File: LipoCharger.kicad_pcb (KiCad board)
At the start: 2 copper layers, 18 parts, among them J1 S2B-XH-A, J2 USB_C_Receptacle_USB2.0_14P, Q1 2300A, Q2 2300A, U1 TP4056-42-ESOP8, U2 DW01A

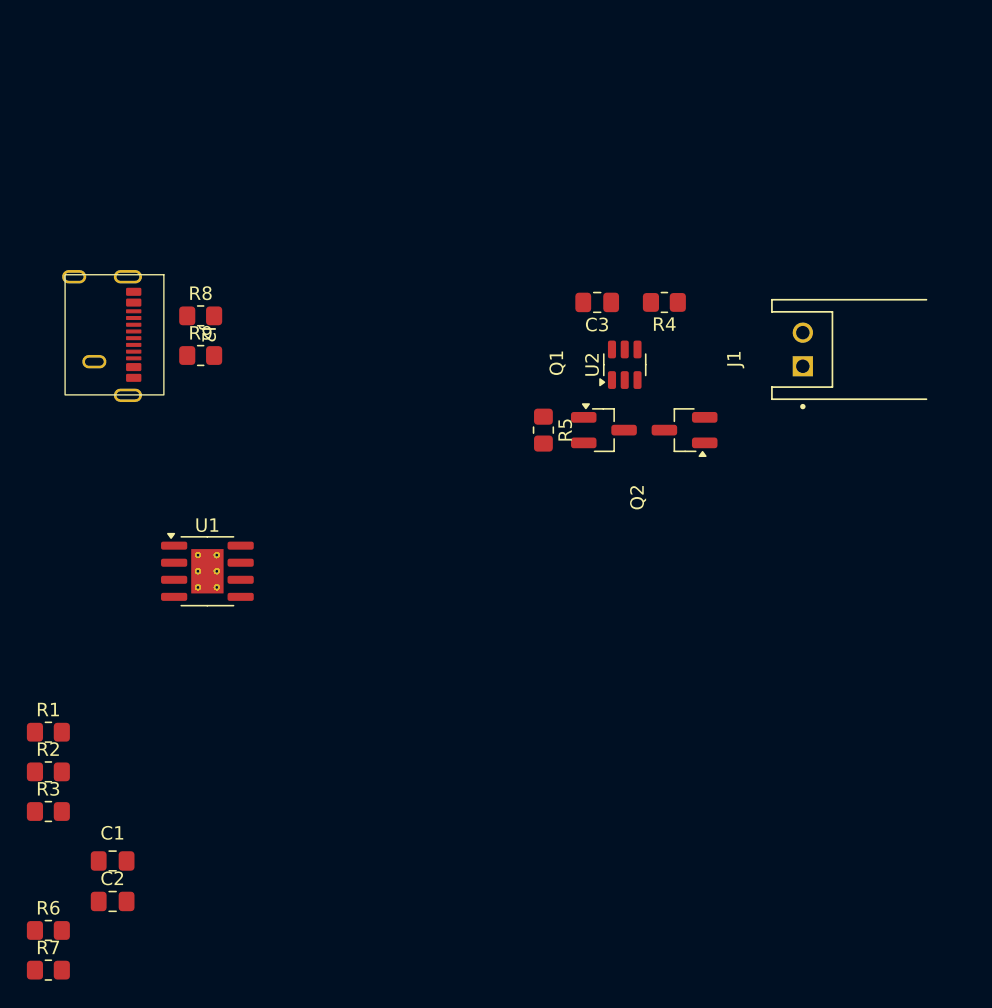
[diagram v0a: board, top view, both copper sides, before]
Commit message: Replaced the DW01 with a FM2113
The DW01 was not suited for a LIPO battery, the under voltage threshold was too low, so it was replaced with the FM2113 which has a much higher threshold
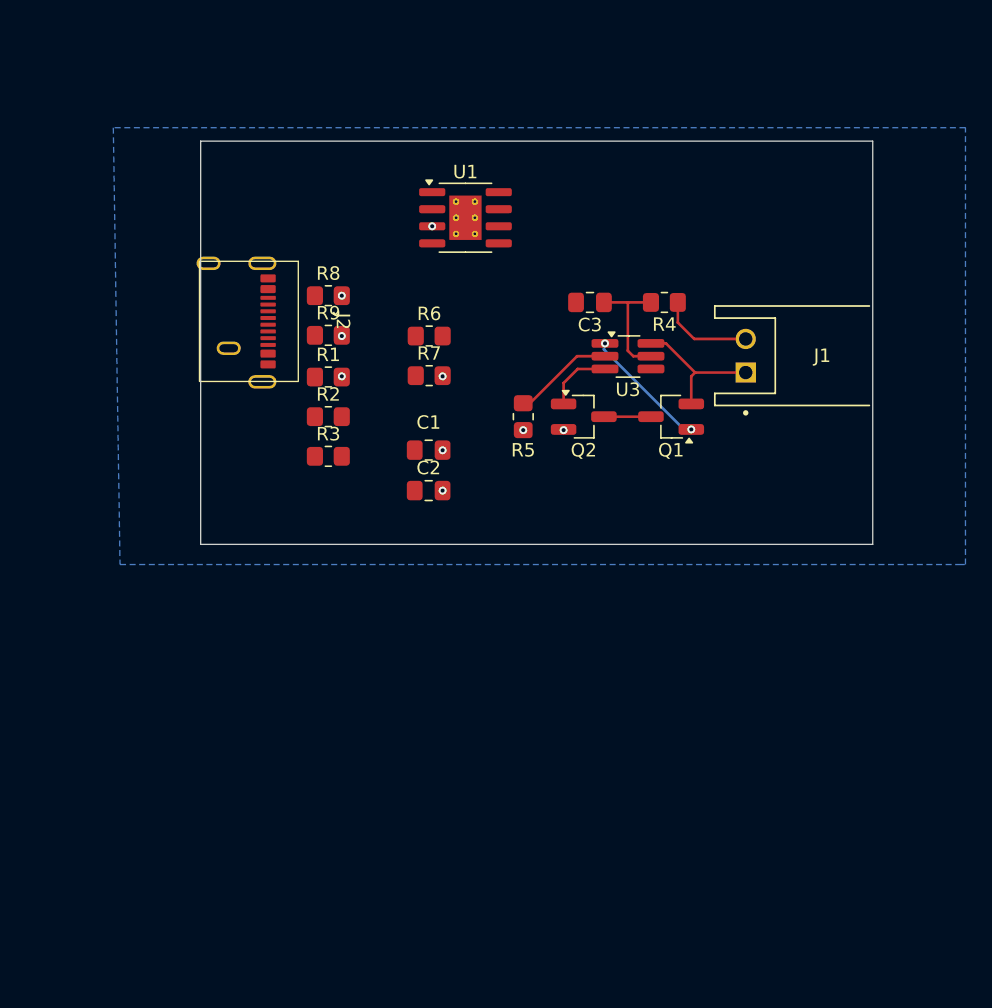
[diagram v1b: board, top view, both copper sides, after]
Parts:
- removed U2: DW01A, Package_TO_SOT_SMD:SOT-23-6
- added U3: FM2113, Package_TO_SOT_SMD:TSOT-23-6_HandSoldering, F.Cu at (61.8, 46.0)
- R5: value 1k -> 2k
- moved R6 52.5 mm to (47.0, 44.5)
- moved R7 52.5 mm to (47.0, 47.5)
- moved C1 38.6 mm to (47.0, 53.0)
- moved C2 38.6 mm to (47.0, 56.0)
- moved R1 33.6 mm to (39.5, 47.5)
- moved R2 33.6 mm to (39.5, 50.5)
- moved R3 33.6 mm to (39.5, 53.5)
- moved U1 32.6 mm to (49.7, 35.7)
- moved J2 10.0 mm to (35.6, 43.4)
- moved R8 9.62 mm to (39.5, 41.5)
- moved R9 9.62 mm to (39.5, 44.5)
- moved Q2 7.57 mm to (58.5, 50.5), turned to 0 degrees
- moved Q1 5.10 mm to (65.0, 50.5), turned to 180 degrees
- moved J1 4.28 mm to (76.2, 46.0)
- moved R5 1.80 mm to (54.0, 50.5)
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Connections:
- net -BATT renamed GND
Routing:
- net Net-(Q1-S): track 0.00 -> 10.4 mm
- net Net-(Q1-G): track 0.00 -> 9.57 mm, vias 0 -> 2
- net Net-(U3-VDD): track 0.00 -> 8.98 mm
- net Net-(U3-CS): track 0.00 -> 7.53 mm
- net +BATT: track 0.00 -> 7.05 mm
- net Net-(Q2-G): track 0.00 -> 5.06 mm
- net Net-(Q1-D): track 0.00 -> 3.50 mm
- net GND: track 0.00 -> 0.28 mm, vias 0 -> 9
- added copper zone on B.Cu, net GND
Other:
- board outline added: 50 x 30 mm

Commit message: Updated usb-c connector, added the 5v switcher, and started to find specific components for the swithcher
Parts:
- added C4: 22uF, Capacitor_SMD:C_0603_1608Metric_Pad1.08x0.95mm_HandSolder, F.Cu at (33.2, 48.8)
- added C5: 22uF, Capacitor_SMD:C_0603_1608Metric_Pad1.08x0.95mm_HandSolder, F.Cu at (33.2, 51.4)
- added D1: RED, LED_SMD:LED_0603_1608Metric_Pad1.05x0.95mm_HandSolder, F.Cu at (41.6, 57.0)
- added D2: GREEN, LED_SMD:LED_0603_1608Metric_Pad1.05x0.95mm_HandSolder, F.Cu at (37.6, 57.0)
- added D3: SS34, Diode_SMD:D_SMA-SMB_Universal_Handsoldering, F.Cu at (63.0, 33.9)
- added H1: MountingHole_Pad, MountingHole:MountingHole_2.2mm_M2_DIN965_Pad, F.Cu at (76.3, 36.9)
- added H2: MountingHole_Pad, MountingHole:MountingHole_2.2mm_M2_DIN965_Pad, F.Cu at (75.5, 55.2)
- added R10: 73.2k, Resistor_SMD:R_0603_1608Metric_Pad0.98x0.95mm_HandSolder, F.Cu at (33.2, 53.9)
- added R11: 10k, Resistor_SMD:R_0603_1608Metric_Pad0.98x0.95mm_HandSolder, F.Cu at (33.2, 56.4)
- added U2: MT3608, Package_TO_SOT_SMD:SOT-23-6, F.Cu at (71.2, 36.8)
- C1, C2, C3: footprint Capacitor_SMD:C_0805_2012Metric_Pad1.18x1.45mm_HandSolder -> Capacitor_SMD:C_0603_1608Metric_Pad1.08x0.95mm_HandSolder
- R1, R2, R3, R4, R5, R6, R7, R8, R9: footprint Resistor_SMD:R_0805_2012Metric_Pad1.20x1.40mm_HandSolder -> Resistor_SMD:R_0603_1608Metric_Pad0.98x0.95mm_HandSolder
- moved J2 3.37 mm to (38.0, 41.0)

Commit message: Cleaned up schematic and added a slide switch
* Added a slide switch for enabling the 5v Switcher
* Added the USB protection and part numbers
* Consolidated all of the symbols into the Symbols folder (instead of the _Library.pretty folder)
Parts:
- added D6: 5.1v, Diode_SMD:Nexperia_CFP3_SOD-123W, F.Cu at (53.1, 45.5)
- added SW1: SK12D07VG4, a_Library:SK12D07VG4 - (SlideSwitch), F.Cu at (33.0, 51.0)
- moved C4 17.5 mm to (50.6, 50.5)
- moved C5 17.5 mm to (50.6, 53.0)
- moved R10 17.5 mm to (50.6, 55.5)
- moved R11 17.5 mm to (50.6, 58.0)
- renumbered H1 to +5v, H2 to GND
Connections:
- net Net-(Q1-S) renamed -BATT
- D3 pad 1: Net-(D3-K) -> +5V
- D3 pad 2: +5V -> Net-(D3-A)
- U2 pad 1: Net-(D3-K) -> Net-(D3-A)

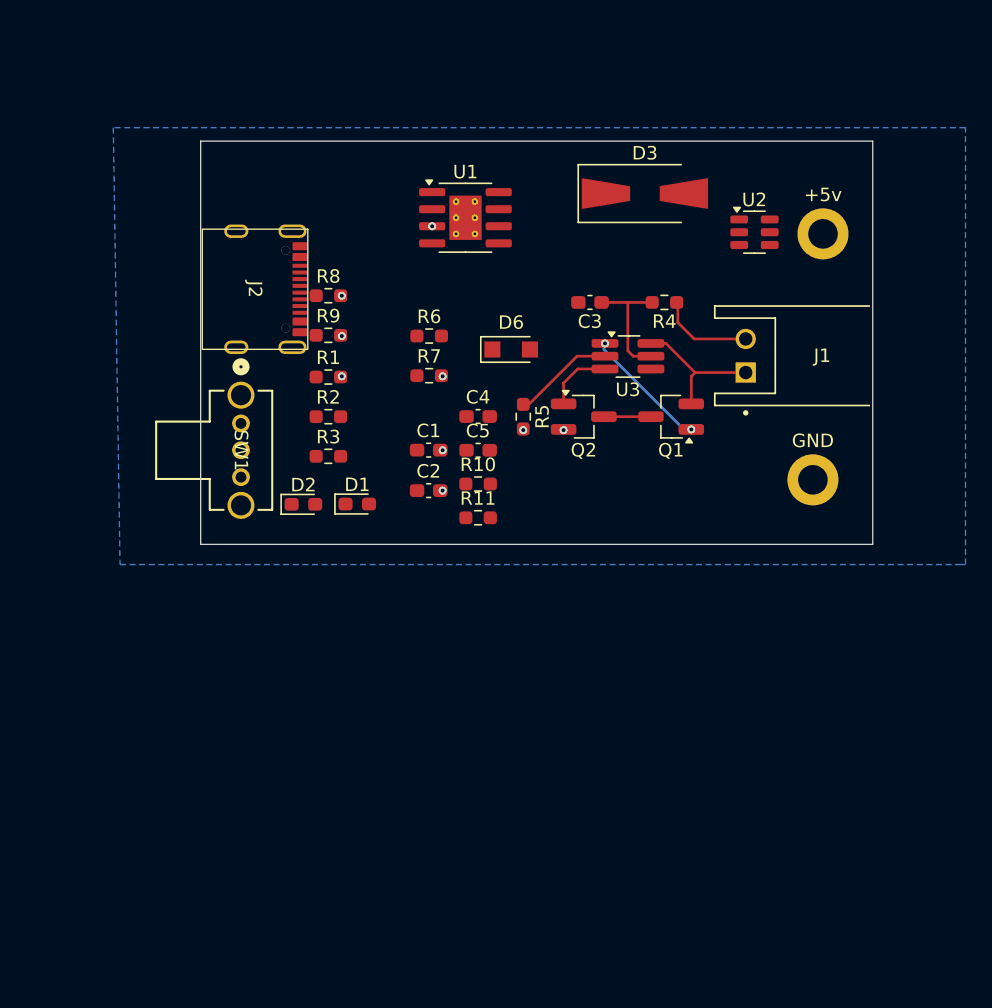
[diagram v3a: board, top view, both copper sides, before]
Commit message: Started laying out the board
Charging circuit should be finalized
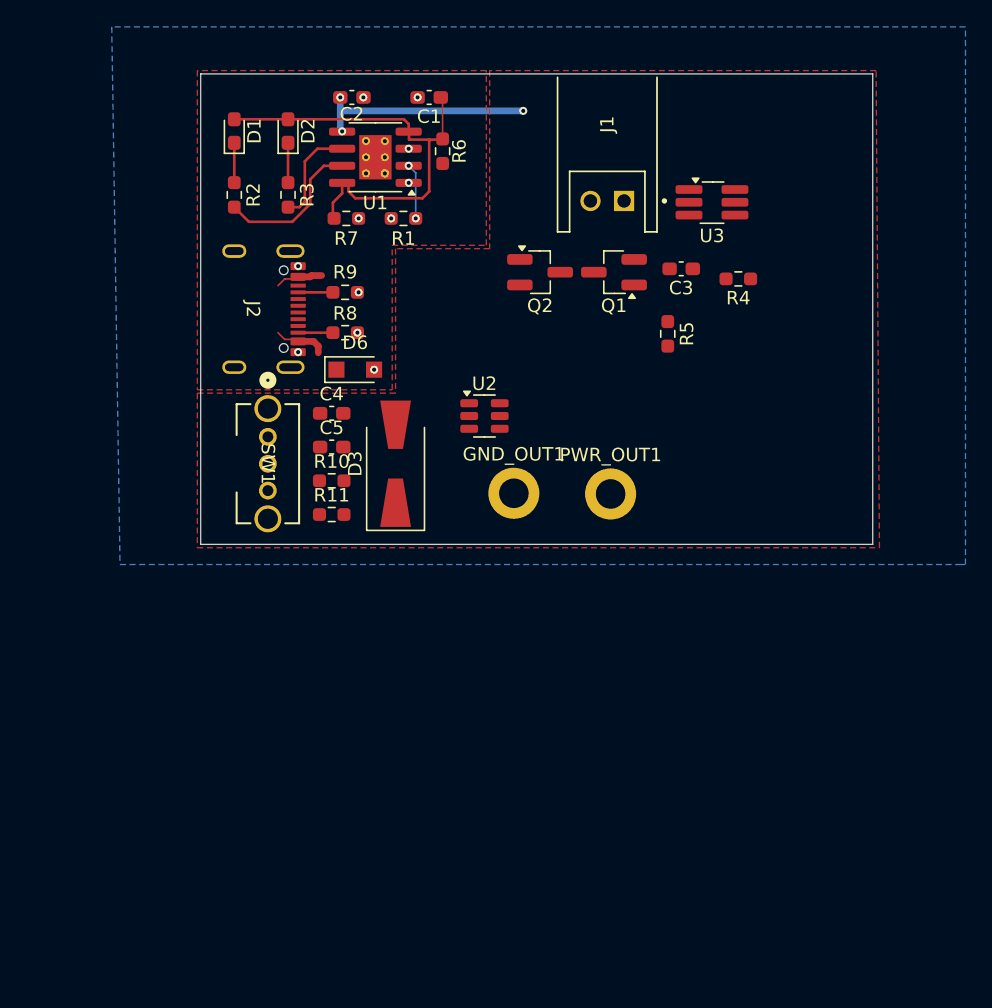
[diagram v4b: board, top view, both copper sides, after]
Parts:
- moved C2 29.8 mm to (41.2, 26.8)
- moved D1 29.2 mm to (32.5, 29.2), turned to 90 degrees
- moved D2 27.8 mm to (36.5, 29.2), turned to 90 degrees
- moved D3 27.4 mm to (44.5, 54.0), turned to 90 degrees
- moved C1 26.2 mm to (47.0, 26.8), turned to 180 degrees
- moved PWR_OUT1 25.0 mm to (60.5, 56.2)
- moved U2 24.3 mm to (51.1, 50.5)
- moved J1 23.5 mm to (60.2, 28.8), turned to 180 degrees
- moved GND_OUT1 22.3 mm to (53.3, 56.2)
- moved R3 19.7 mm to (36.5, 34.0), turned to -90 degrees
- moved R2 17.9 mm to (32.5, 34.0), turned to -90 degrees
- moved R6 13.8 mm to (48.0, 30.8), turned to 90 degrees
- moved R7 13.2 mm to (40.8, 35.8)
- moved R1 13.1 mm to (45.1, 35.8), turned to 180 degrees
- moved U3 13.0 mm to (68.0, 34.5)
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- renumbered GND to GND_OUT1, +5v to PWR_OUT1
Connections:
- net +5V renamed Net-(D3-K)
- SW1 pad 1: unconnected-(SW1-Pad1) -> GND
- SW1 pad 2: unconnected-(SW1-Pad2) -> Net-(U2-EN)
- SW1 pad 3: unconnected-(SW1-Pad3) -> +BATT
- U2 pad 4: unconnected-(U2-EN-Pad4) -> Net-(U2-EN)
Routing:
- net Net-(D1-A): track 0.00 -> 34.2 mm
- net Net-(U1-~{CHRG}): track 0.00 -> 11.3 mm
- net -BATT: track 10.4 -> 0.00 mm
- net Net-(Q1-G): track 9.57 -> 0.00 mm, vias 2 -> 0
- net +BATT: track 7.05 -> 16.4 mm, vias 0 -> 3
- net Net-(U3-VDD): track 8.98 -> 0.00 mm
- net Net-(U1-~{STDBY}): track 0.00 -> 7.58 mm
- net Net-(U3-CS): track 7.53 -> 0.00 mm
- net VBUS: track 0.00 -> 7.47 mm
- net Net-(Q2-G): track 5.06 -> 0.00 mm
- net Net-(U1-PROG): track 0.00 -> 4.27 mm, vias 0 -> 2
- net Net-(Q1-D): track 3.50 -> 0.00 mm
- net Net-(D2-K): track 0.00 -> 2.96 mm
- net Net-(D1-K): track 0.00 -> 2.96 mm
- net Net-(J2-CC2): track 0.00 -> 2.59 mm
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- added copper zone on F.Cu, net +BATT
- added copper zone on F.Cu, net VBUS
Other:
- board size 50 x 30 mm -> 50 x 35 mm
- copper layers 2 -> 4

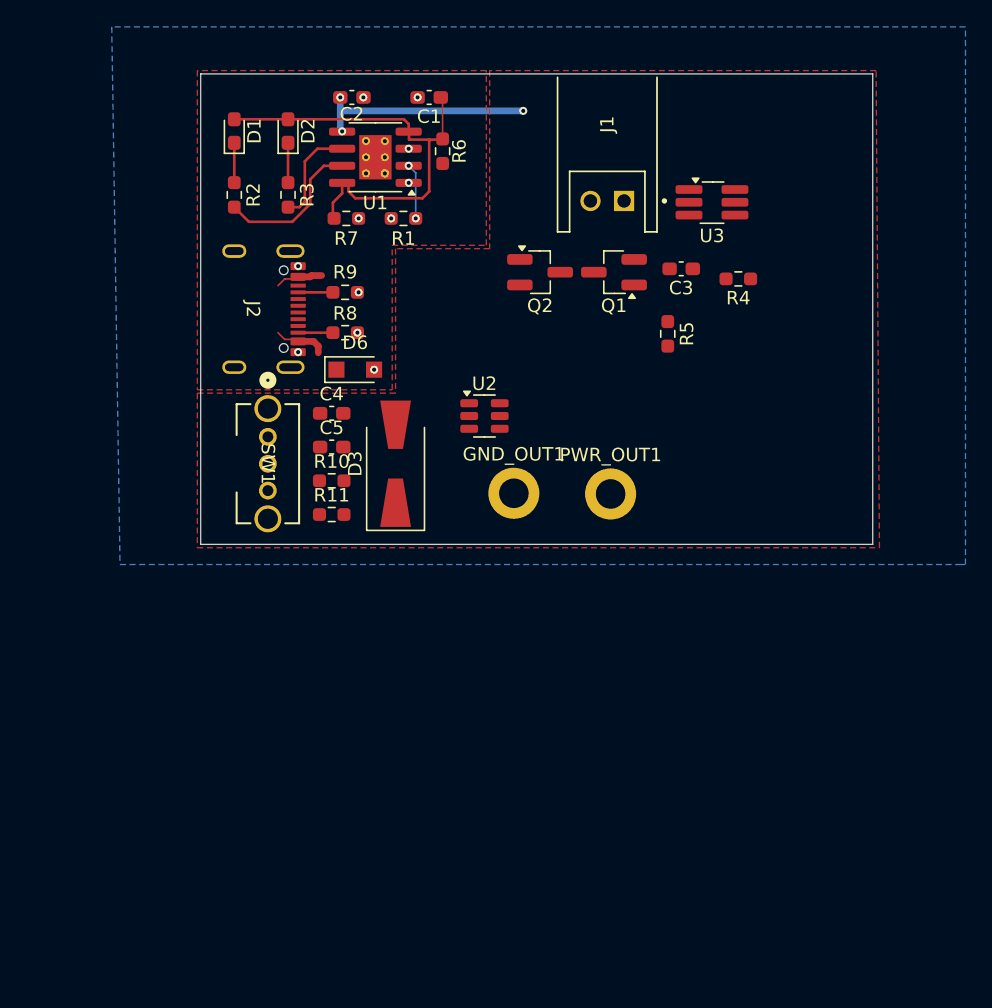
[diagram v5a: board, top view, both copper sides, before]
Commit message: Finished Layout and routing, just need to add mounting holes
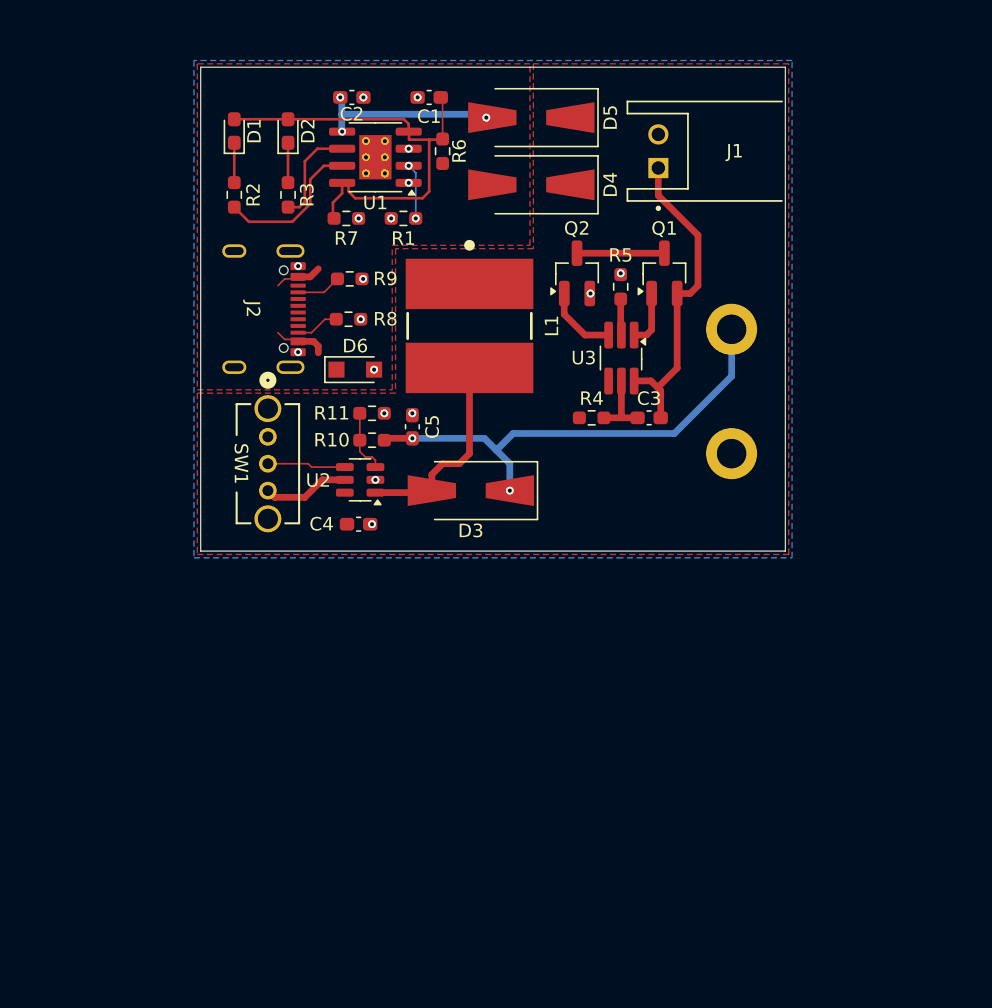
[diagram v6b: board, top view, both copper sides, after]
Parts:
- added D4: B340A, Diode_SMD:D_SMA-SMB_Universal_Handsoldering, F.Cu at (54.6, 33.2)
- added D5: B340A, Diode_SMD:D_SMA-SMB_Universal_Handsoldering, F.Cu at (54.6, 28.2)
- added L1: 22uH, a_Library:WE-PD2_1054, F.Cu at (50.0, 43.8)
- Q1, Q2: value 2300A -> SI2300A
- moved GND_OUT1 16.5 mm to (69.5, 53.2)
- moved PWR_OUT1 15.2 mm to (69.5, 44.0)
- moved R4 15.0 mm to (59.1, 50.6), turned to 0 degrees
- moved U3 13.4 mm to (61.3, 46.1), turned to -90 degrees
- moved C3 11.3 mm to (63.4, 50.6), turned to 0 degrees
- moved U2 10.4 mm to (41.9, 55.2), turned to 180 degrees
- moved J1 9.71 mm to (69.8, 30.8), turned to 90 degrees
- moved C4 8.49 mm to (41.8, 58.5)
- moved R11 8.11 mm to (42.8, 50.2)
- moved C5 6.19 mm to (45.8, 51.2), turned to 90 degrees
- moved D3 5.95 mm to (50.1, 56.0), turned to 180 degrees
- moved R5 4.95 mm to (61.2, 40.8), turned to 90 degrees
- moved R10 4.26 mm to (42.8, 52.2), turned to 180 degrees
- moved Q1 3.75 mm to (64.5, 39.8), turned to 90 degrees
- moved Q2 2.75 mm to (58.0, 39.8), turned to 90 degrees
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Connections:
- C2 pad 1: +BATT -> Net-(D5-A)
- U1 pad 5: +BATT -> Net-(D5-A)
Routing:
- net Net-(D3-K): track 0.00 -> 35.5 mm, vias 0 -> 2
- net -BATT: track 0.00 -> 23.9 mm
- net Net-(D3-A): track 0.00 -> 14.1 mm
- net Net-(D5-A): track 0.00 -> 13.6 mm, vias 0 -> 3
- net +BATT: track 16.4 -> 6.47 mm, vias 3 -> 0
- net Net-(Q1-D): track 0.00 -> 6.50 mm
- net Net-(U2-EN): track 0.00 -> 5.83 mm
- net Net-(Q2-G): track 0.00 -> 5.49 mm
- net Net-(U3-VDD): track 0.00 -> 5.26 mm
- net Net-(U2-FB): track 0.00 -> 4.77 mm
- net Net-(Q1-G): track 0.00 -> 4.16 mm
- net Net-(U3-CS): track 0.00 -> 2.70 mm
- net Net-(J2-CC1): track 2.59 -> 3.34 mm
- net Net-(J2-CC2): track 2.59 -> 3.25 mm
- net GND: track 0.19 -> 0.65 mm, vias 11 -> 17
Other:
- board size 50 x 35 mm -> 43.5 x 36 mm

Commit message: Made some small changes and added my "Logo"
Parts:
- added Devin M.: LOGO, a_Library:PCB Logo (12.5x17), B.Cu at (62.0, 51.0)
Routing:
- net Net-(D3-K): track 35.5 -> 36.6 mm
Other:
- board text added: "+5V"
- board text added: "Devin Marx"
- board text added: "GND"
- board text added: "LiPo Charger/Protection Board with 5v/2A Output"
